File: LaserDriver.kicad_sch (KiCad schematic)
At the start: 16 parts, among them J100 Screw_Terminal_01x02, J101 Screw_Terminal_01x02, J102 Screw_Terminal_01x02, U1 TPS92513DGQR

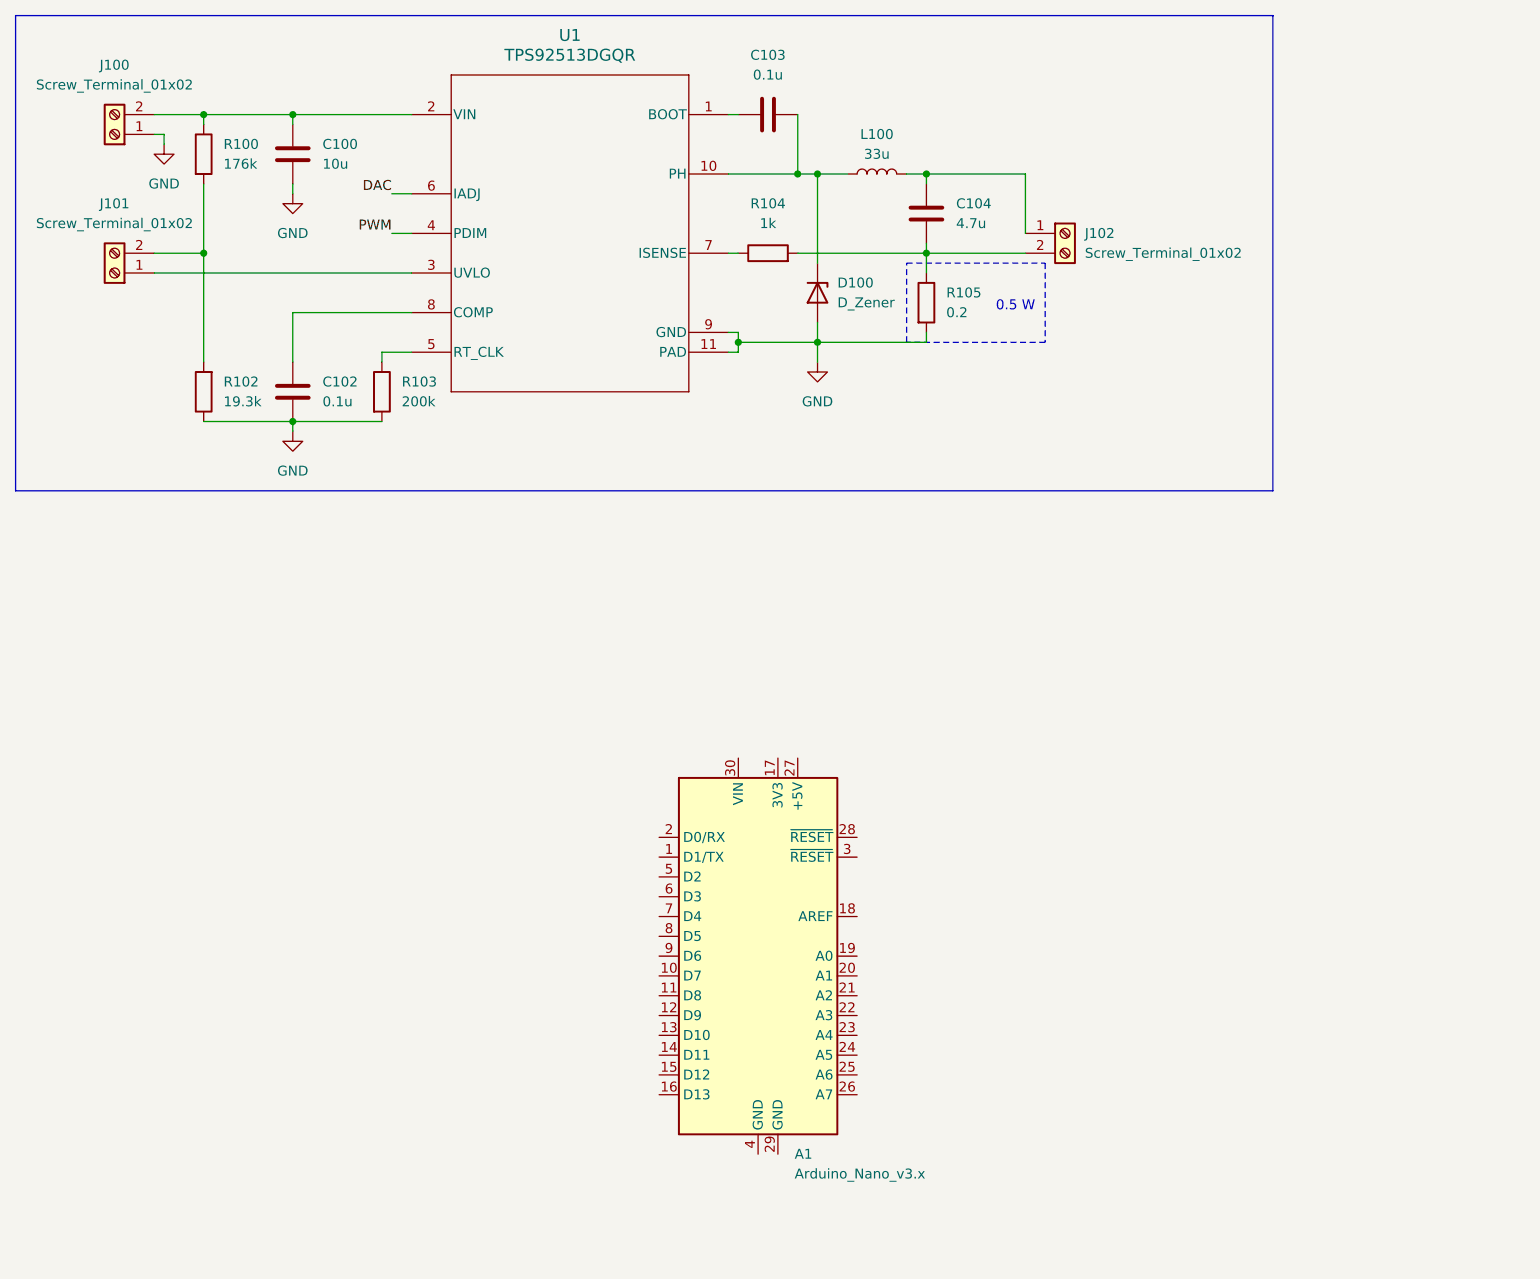
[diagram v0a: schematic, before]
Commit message: added arduino
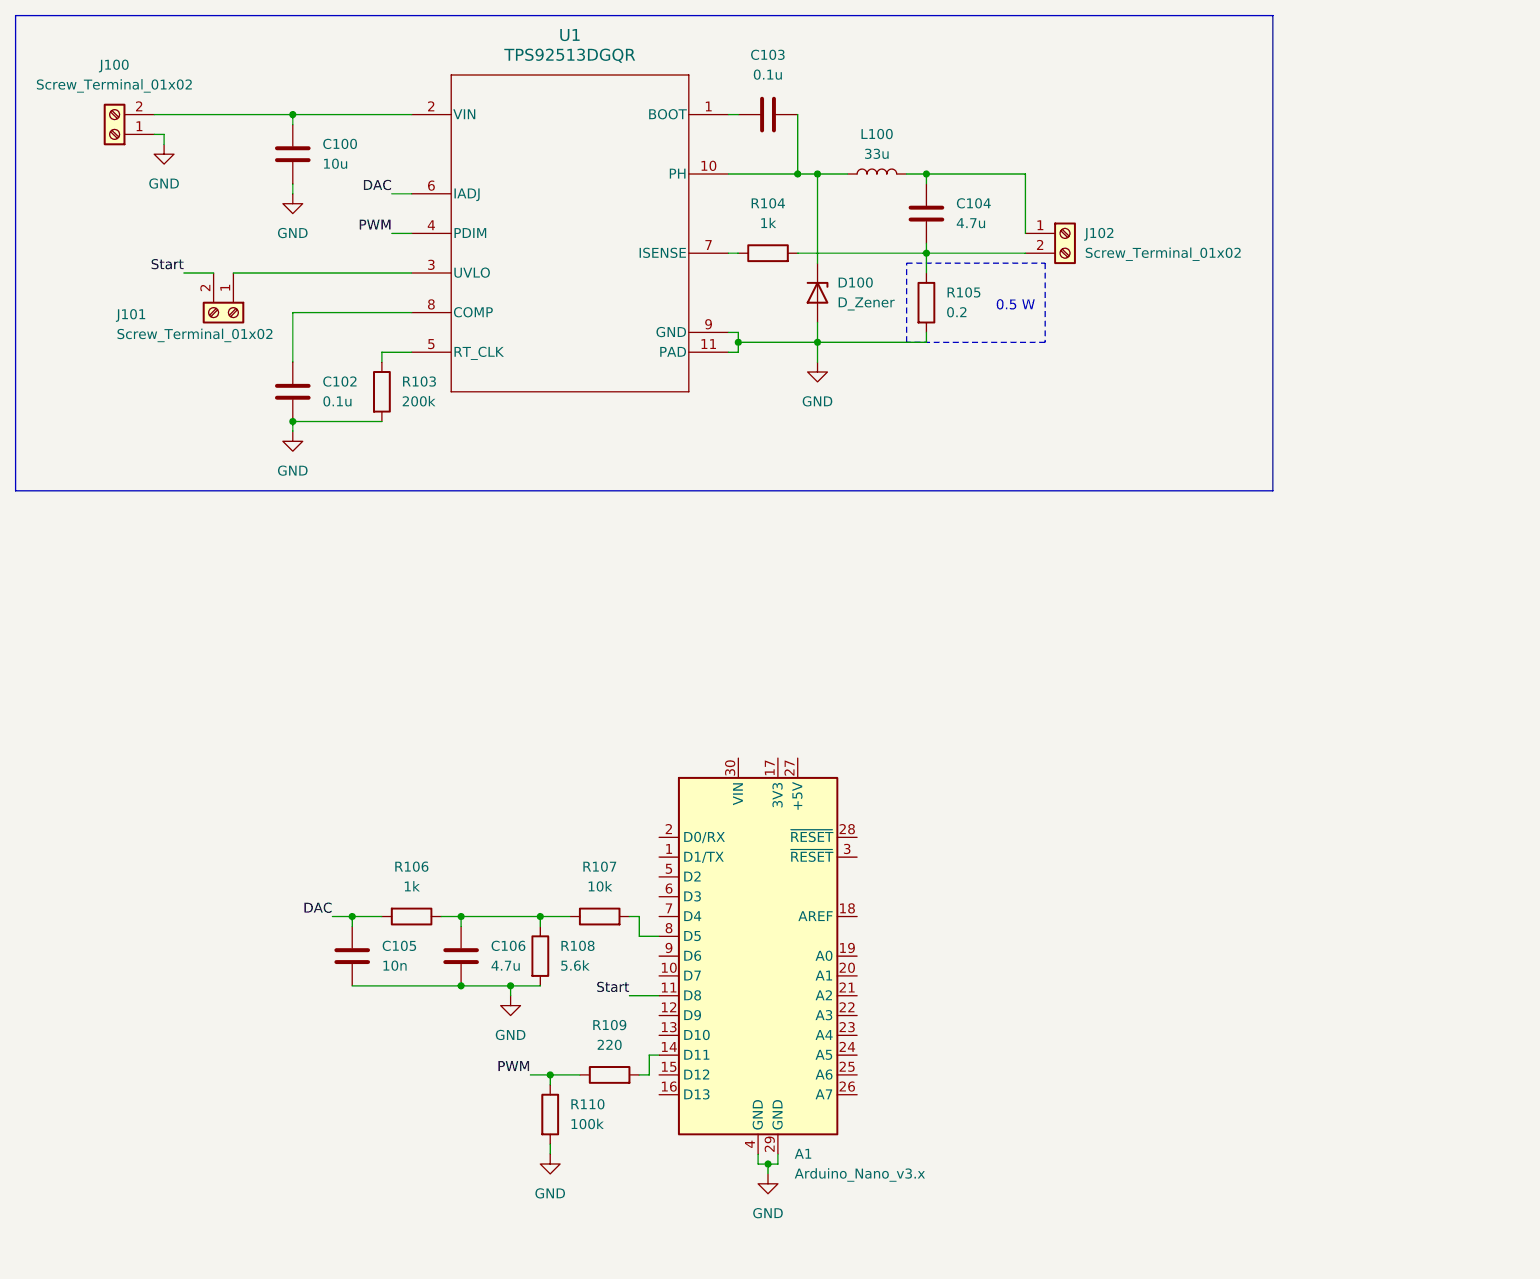
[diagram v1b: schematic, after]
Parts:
- removed R100: 176k, symbol Device:R
- removed R102: 19.3k, symbol Device:R
- added C105: 10n, symbol Device:C
- added C106: 4.7u, symbol Device:C
- added R106: 1k, symbol Device:R
- added R107: 10k, symbol Device:R
- added R108: 5.6k, symbol Device:R
- added R109: 220, symbol Device:R
- added R110: 100k, symbol Device:R
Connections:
- net DAC: now also C105.1, R106.2
- net GND: now also A1.29 (GND), A1.4 (GND), C105.2, C106.2, R108.2, R110.2
- net PWM: now also R109.1, R110.1
- net Start: now reaches J101.2 (Pin_2)
- net Start: now also A1.11 (D8)
- net at A1.14 (D11): now also R109.2
- net at A1.8 (D5): now also R107.2
- new net: C106.1, R106.1, R107.1, R108.1
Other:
- moved on the sheet: J101

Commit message: started footprints
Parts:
- C100: footprint (none) -> Capacitor_SMD:C_1206_3216Metric
- C102, C103, C105: footprint (none) -> Capacitor_SMD:C_0603_1608Metric
- C104, C106: footprint (none) -> Capacitor_SMD:C_0805_2012Metric
- D100: footprint (none) -> Diode_SMD:D_SMB
- J100, J101, J102: footprint (none) -> TerminalBlock:TerminalBlock_MaiXu_MX126-5.0-02P_1x02_P5.00mm
- U1: footprint DGQ0010D_NV_N -> (none)
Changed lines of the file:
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@@
 			)
 		)
-		(property "Footprint" ""
+		(property "Footprint" "Capacitor_SMD:C_0805_2012Metric"
 			(at 134.3152 45.72 0)
 			(effects
@@
 			)
 		)
-		(property "Footprint" ""
+		(property "Footprint" "TerminalBlock:TerminalBlock_MaiXu_MX126-5.0-02P_1x02_P5.00mm"
 			(at 151.13 44.45 0)
 			(effects
@@
 			)
 		)
-		(property "Footprint" ""
+		(property "Footprint" "Capacitor_SMD:C_0603_1608Metric"
 			(at 53.0352 68.58 0)
 			(effects
@@
 			)
 		)
-		(property "Footprint" ""
+		(property "Footprint" "Capacitor_SMD:C_0603_1608Metric"
 			(at 60.6552 140.97 0)
 			(effects
@@
 			)
 		)
-		(property "Footprint" ""
+		(property "Footprint" "TerminalBlock:TerminalBlock_MaiXu_MX126-5.0-02P_1x02_P5.00mm"
 			(at 29.21 31.75 0)
 			(effects
@@
 			)
 		)
-		(property "Footprint" ""
+		(property "Footprint" "Capacitor_SMD:C_0603_1608Metric"
 			(at 116.84 28.2448 0)
 			(effects
@@
 			)
 		)
-		(property "Footprint" ""
+		(property "Footprint" "TerminalBlock:TerminalBlock_MaiXu_MX126-5.0-02P_1x02_P5.00mm"
 			(at 44.45 54.61 0)
 			(effects
@@
 			)
 		)
-		(property "Footprint" "DGQ0010D_NV_N"
+		(property "Footprint" ""
 			(at 87.63 44.45 0)
 			(effects
@@
 			)
 		)
-		(property "Footprint" ""
+		(property "Footprint" "Capacitor_SMD:C_1206_3216Metric"
 			(at 53.0352 38.1 0)
 			(effects
@@
 			)
 		)
-		(property "Footprint" ""
+		(property "Footprint" "Diode_SMD:D_SMB"
 			(at 119.38 52.07 0)
 			(effects
@@
 			)
 		)
-		(property "Footprint" ""
+		(property "Footprint" "Capacitor_SMD:C_0805_2012Metric"
 			(at 74.6252 140.97 0)
 			(effects

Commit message: Started pcb editor
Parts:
- L100: footprint (none) -> Inductor_SMD:L_7.3x7.3_H4.5
- R103, R104, R106, R107, R108, R109, R110: footprint (none) -> Resistor_SMD:R_0603_1608Metric
- R105: footprint (none) -> Resistor_SMD:R_2512_6332Metric
- U1: footprint (none) -> TPS:DGQ0010D_M
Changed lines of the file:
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@@
 			)
 		)
-		(property "Footprint" ""
+		(property "Footprint" "Resistor_SMD:R_0603_1608Metric"
 			(at 91.44 133.858 90)
 			(effects
@@
 			)
 		)
-		(property "Footprint" ""
+		(property "Footprint" "Resistor_SMD:R_0603_1608Metric"
 			(at 92.71 154.178 90)
 			(effects
@@
 			)
 		)
-		(property "Footprint" ""
+		(property "Footprint" "Resistor_SMD:R_0603_1608Metric"
 			(at 113.03 48.768 90)
 			(effects
@@
 			)
 		)
-		(property "Footprint" ""
+		(property "Footprint" "Resistor_SMD:R_2512_6332Metric"
 			(at 131.572 53.34 90)
 			(effects
@@
 			)
 		)
-		(property "Footprint" ""
+		(property "Footprint" "Resistor_SMD:R_0603_1608Metric"
 			(at 82.042 137.16 90)
 			(effects
@@
 			)
 		)
-		(property "Footprint" ""
+		(property "Footprint" "Resistor_SMD:R_0603_1608Metric"
 			(at 67.31 130.302 90)
 			(effects
@@
 			)
 		)
-		(property "Footprint" ""
+		(property "Footprint" "Resistor_SMD:R_0603_1608Metric"
 			(at 83.312 157.48 90)
 			(effects
@@
 			)
 		)
-		(property "Footprint" ""
+		(property "Footprint" "Inductor_SMD:L_7.3x7.3_H4.5"
 			(at 127 36.83 0)
 			(effects
@@
 			)
 		)
-		(property "Footprint" ""
+		(property "Footprint" "Resistor_SMD:R_0603_1608Metric"
 			(at 61.722 64.77 90)
 			(effects
@@
 			)
 		)
-		(property "Footprint" ""
+		(property "Footprint" "TPS:DGQ0010D_M"
 			(at 87.63 44.45 0)
 			(effects

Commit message: add arduino 3d model
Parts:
- A1: footprint Module:Arduino_Nano -> Arduino:Arduino_Nano
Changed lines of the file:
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@@
 			)
 		)
-		(property "Footprint" "Module:Arduino_Nano"
+		(property "Footprint" "Arduino:Arduino_Nano"
 			(at 111.76 137.16 0)
 			(effects

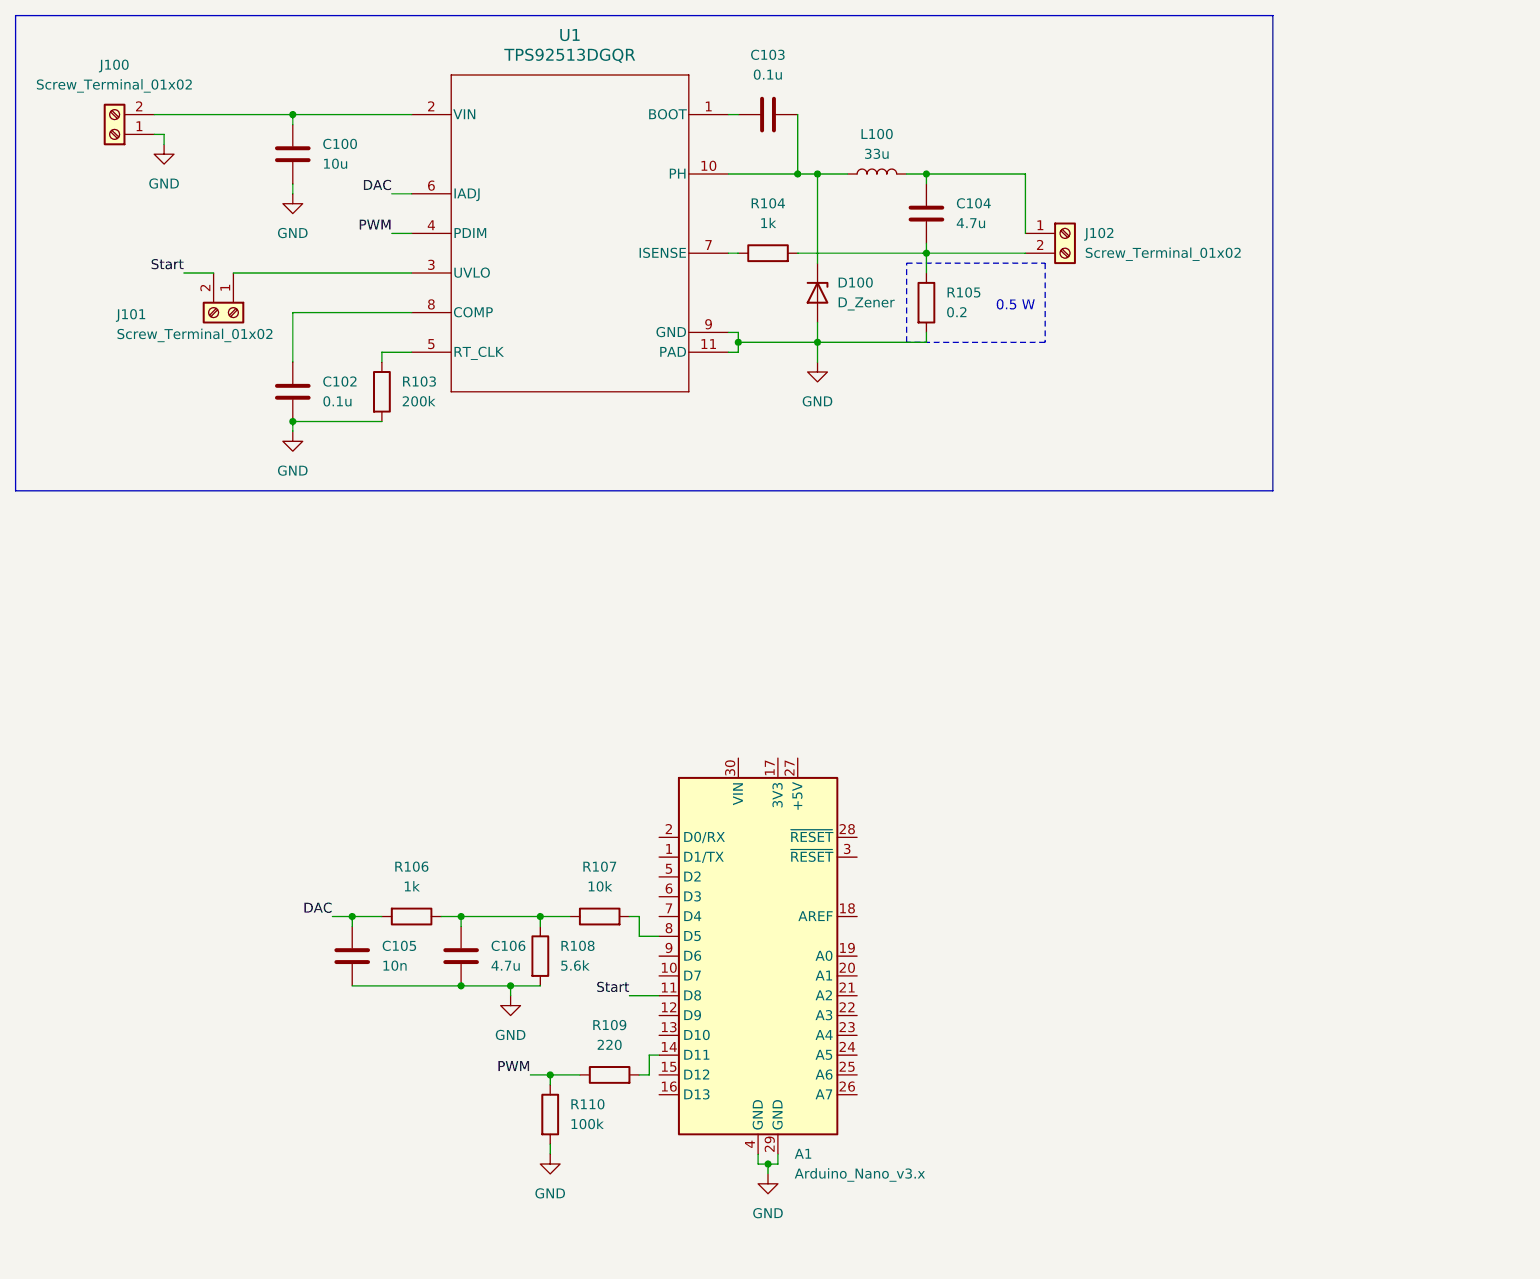
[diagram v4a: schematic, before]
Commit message: added esd protection
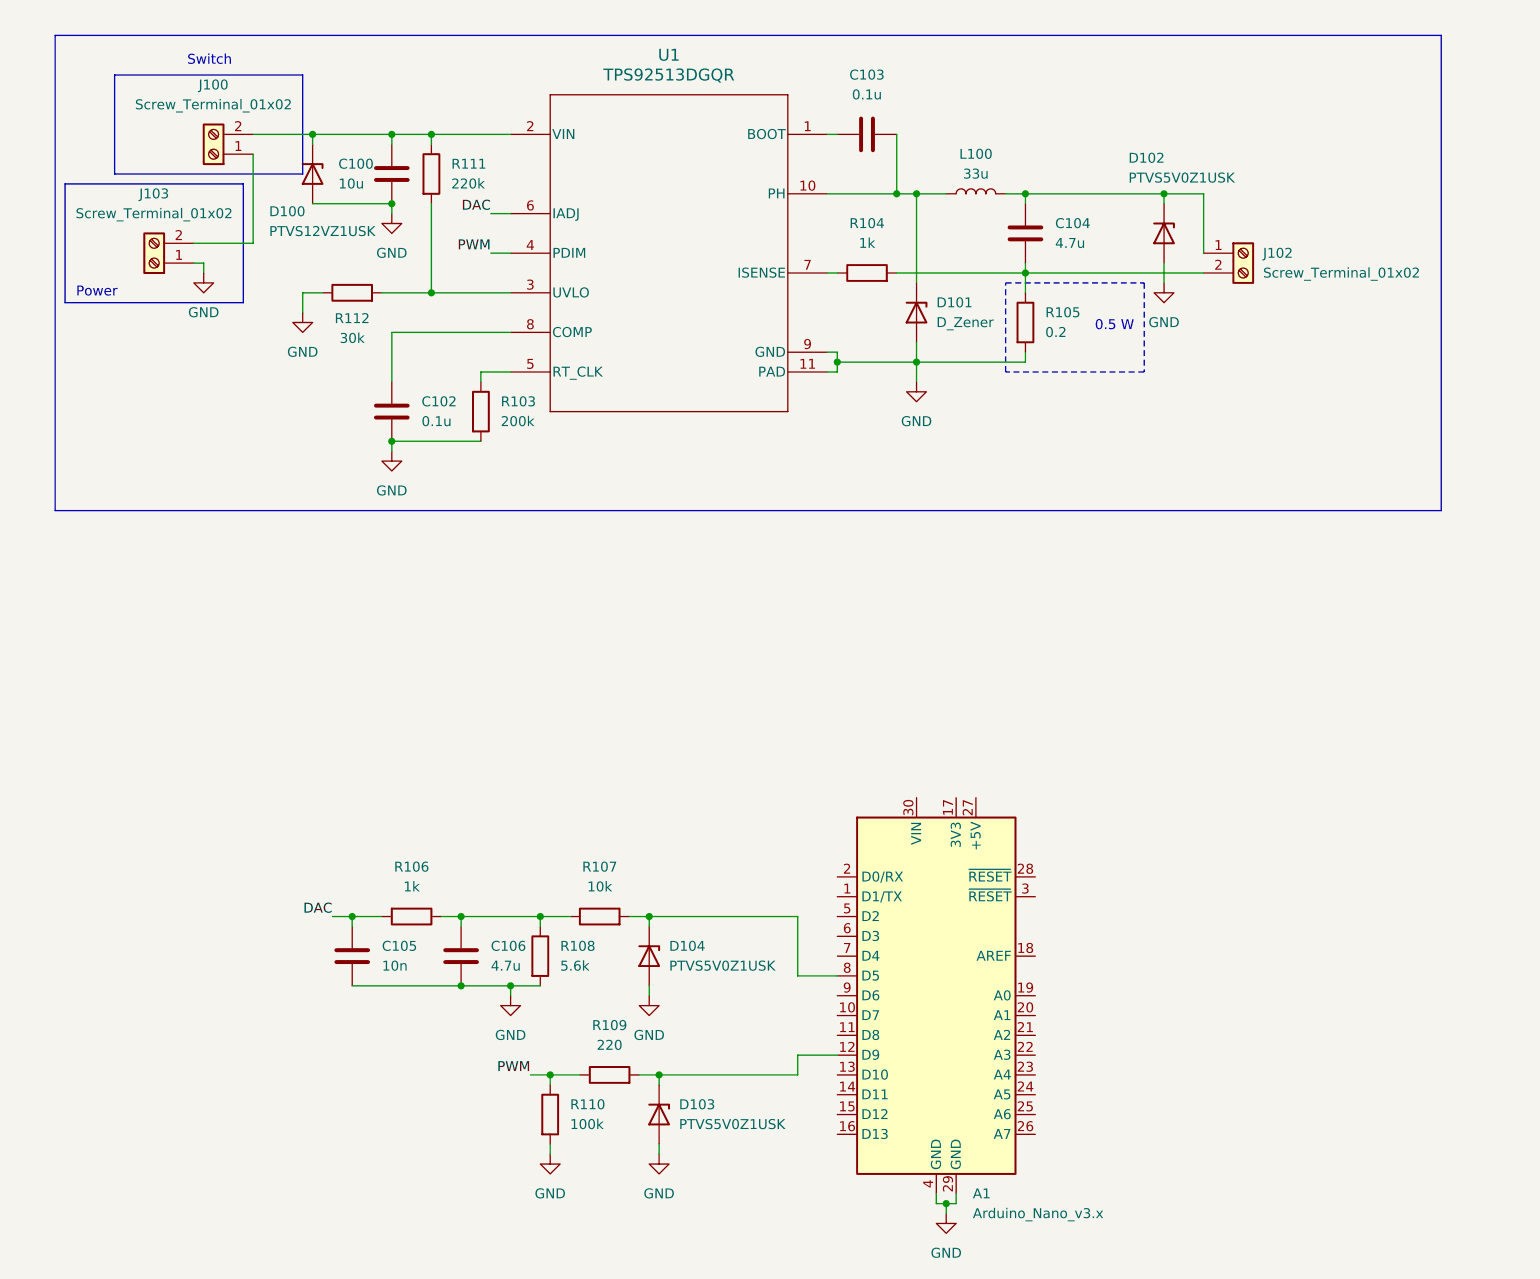
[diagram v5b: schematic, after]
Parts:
- removed J101: Screw_Terminal_01x02, TerminalBlock:TerminalBlock_MaiXu_MX126-5.0-02P_1x02_P5.00mm, symbol Connector:Screw_Terminal_01x02
- added D100: PTVS12VZ1USK, Diode_SMD:Nexperia_DSN1608-2_1.6x0.8mm, symbol Diode:PTVS12VZ1USK
- added D102, D103, D104: PTVS5V0Z1USK, Diode_SMD:Nexperia_DSN1608-2_1.6x0.8mm, symbol Diode:PTVS5V0Z1USK
- added J103: Screw_Terminal_01x02, TerminalBlock:TerminalBlock_MaiXu_MX126-5.0-02P_1x02_P5.00mm, symbol Connector:Screw_Terminal_01x02
- added R111: 220k, Resistor_SMD:R_0603_1608Metric, symbol Device:R
- added R112: 30k, Resistor_SMD:R_0603_1608Metric, symbol Device:R
- renumbered D100 to D101
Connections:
- net GND: now also D100.2 (A), D102.2 (A), D103.2 (A), D104.2 (A), J103.1 (Pin_1), R112.1; no longer J100.1 (Pin_1)
- net at A1.8 (D5), R107.2: now also D104.1 (K)
- net at R109.2: now also A1.12 (D9), D103.1 (K); no longer A1.14 (D11)
- net at C104.1, J102.1 (Pin_1), L100.2: now also D102.1 (K)
- net at C100.1, J100.2 (Pin_2), U1.2 (VIN): now also D100.1 (K), R111.1
- net at U1.3 (UVLO): now also R111.2, R112.2
- net Start: no longer names the net of A1.11 (D8)
- new net: J100.1 (Pin_1), J103.2 (Pin_2)
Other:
- note added: "Power"
- note added: "Switch"
- moved on the sheet: A1, C100, C102, C103, C104, D101, J100, J102, L100, R103, R104, R105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

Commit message: power changes
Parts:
- U1: footprint TPS:DGQ0010D_M -> TPS:DGQ0010D_L

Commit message: compactified design
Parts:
- removed J100, J103: Screw_Terminal_01x02, TerminalBlock:TerminalBlock_MaiXu_MX126-5.0-02P_1x02_P5.00mm, symbol Connector:Screw_Terminal_01x02
- added J100: Screw_Terminal_01x04, TerminalBlock:TerminalBlock_MaiXu_MX126-5.0-04P_1x04_P5.00mm, symbol Connector:Screw_Terminal_01x04
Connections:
- net GND: now also J100.1 (Pin_1)
- net at C100.1, D100.1 (K), R111.1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: now also J100.4 (Pin_4)
- new net: J100.2 (Pin_2), J100.3 (Pin_3)
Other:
- note removed: "Power"
- note removed: "Switch"
